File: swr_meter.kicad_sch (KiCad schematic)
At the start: 15 parts, among them U301 LTC5507, U302 LTC5507

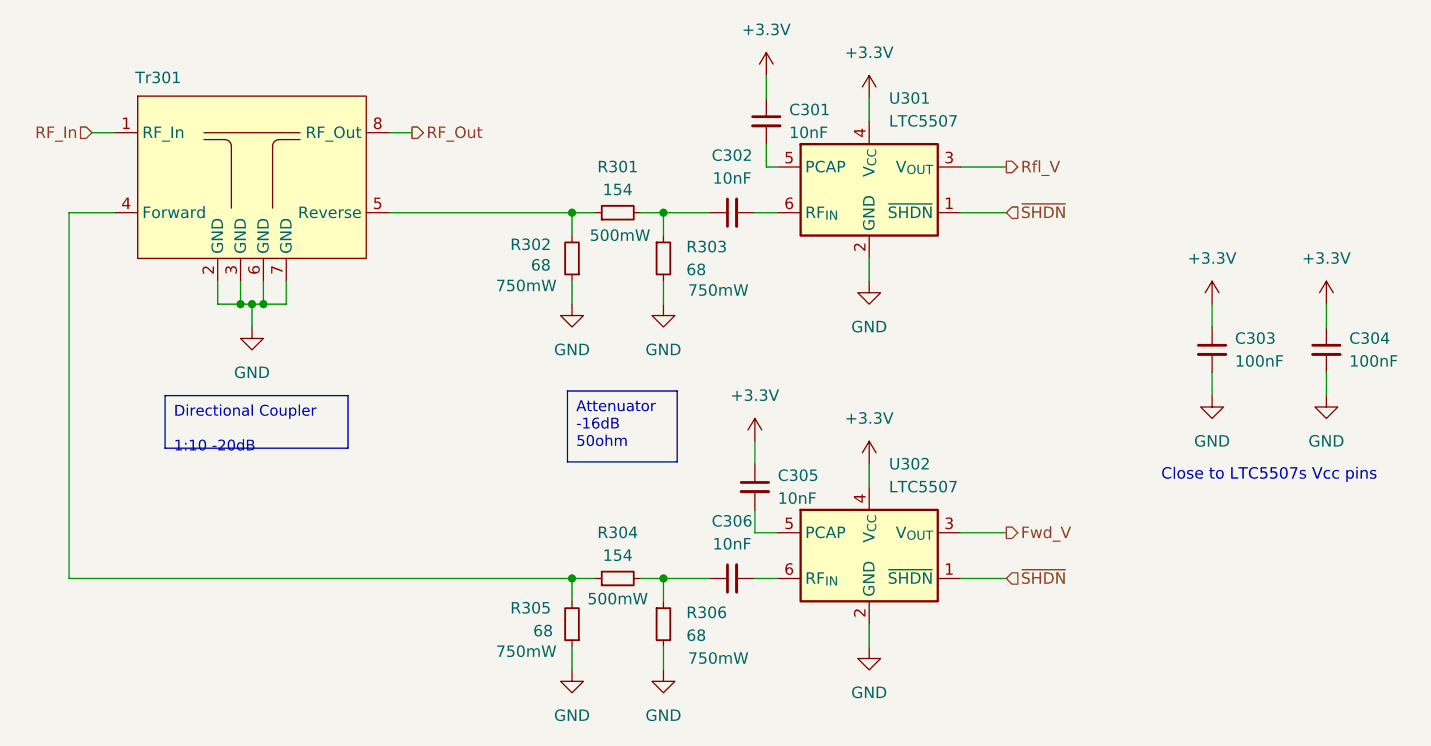
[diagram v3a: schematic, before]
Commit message: A0 Production. Updated to KiCad 9.0.x
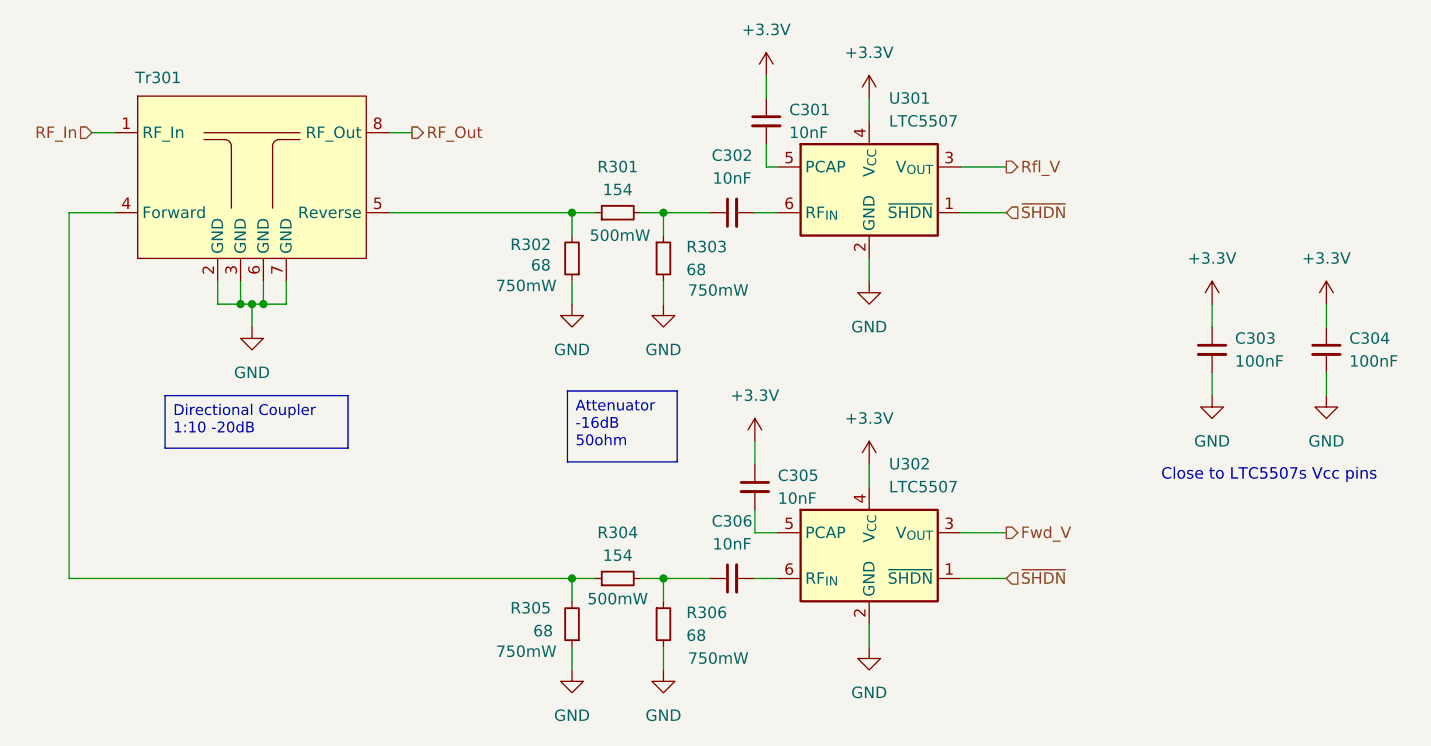
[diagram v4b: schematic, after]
